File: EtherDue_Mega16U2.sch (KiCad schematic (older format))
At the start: 25 parts, among them IC301 ATMEGA16U2, P301 USB_5PIN_SHELL, X301 TXC 7A 12MHz 18pF

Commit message: Pre-autorouter hand routed traces
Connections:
- net labels added: RD+_CONN, RD-_CONN, USBVCCU2_CONN
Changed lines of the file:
@@
-EESchema Schematic File Version 2  date Thu 06 Jun 2013 17:31:40 EST
+EESchema Schematic File Version 2  date Wed 19 Jun 2013 10:44:48 EST
 LIBS:freetronics_kicad_sch_lib
 LIBS:power
@@
 Sheet 3 6
 Title ""
-Date "6 jun 2013"
+Date "19 jun 2013"
 Rev ""
 Comp ""
@@
 NoConn ~ 8100 2400
 NoConn ~ 8100 2500
+Text Label 2600 4250 2    60   ~ 0
+RD-_CONN
+Text Label 2600 4450 2    60   ~ 0
+RD+_CONN
+Text Label 1450 4150 0    60   ~ 0
+USBVCCU2_CONN
 $EndSCHEMATC

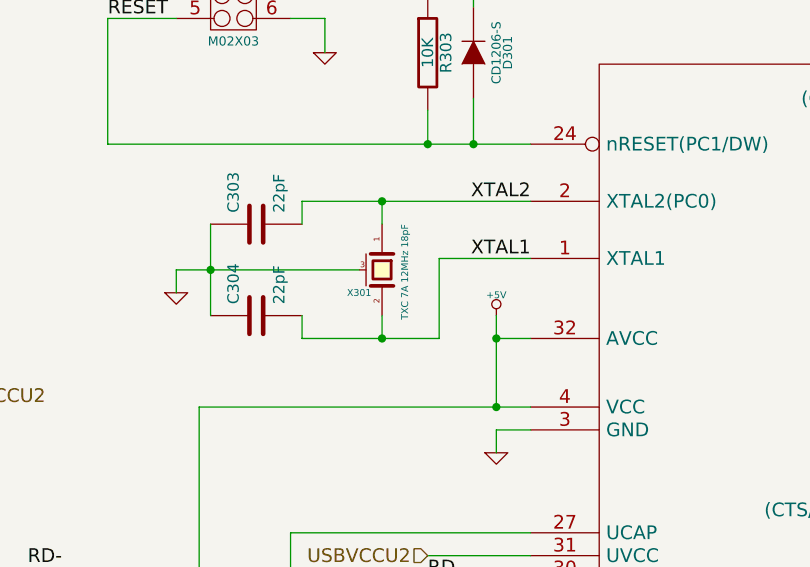
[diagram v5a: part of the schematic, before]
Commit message: Fix ATMega16u2 to run at 16MHz
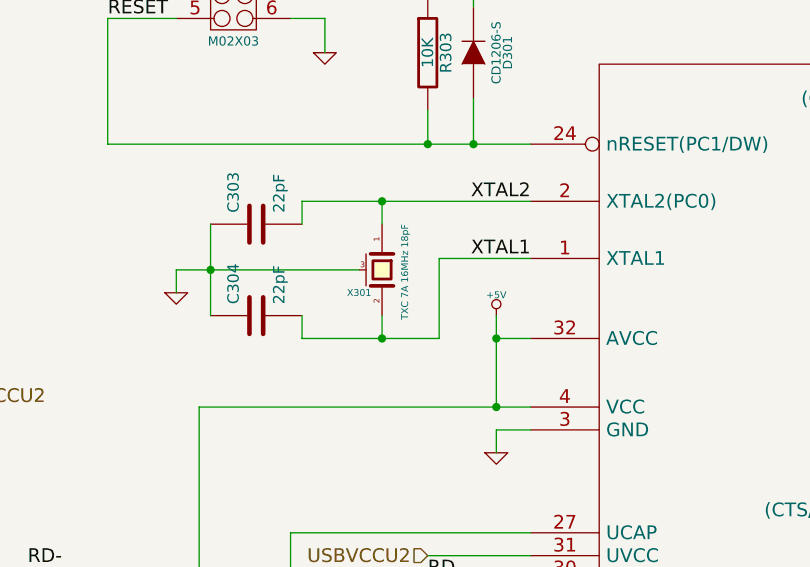
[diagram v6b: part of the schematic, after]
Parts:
- X301: value TXC 7A 12MHz 18pF -> TXC 7A 16MHz 18pF
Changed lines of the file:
@@
 P 4900 2950
 F 0 "X301" V 5000 2850 30  0000 C CNN
-F 1 "TXC 7A 12MHz 18pF" H 4700 3050 30  0000 L CNN
+F 1 "TXC 7A 16MHz 18pF" H 4700 3050 30  0000 L CNN
 F 2 "~" H 4900 2950 60  0000 C CNN
 F 3 "~" H 4900 2950 60  0000 C CNN

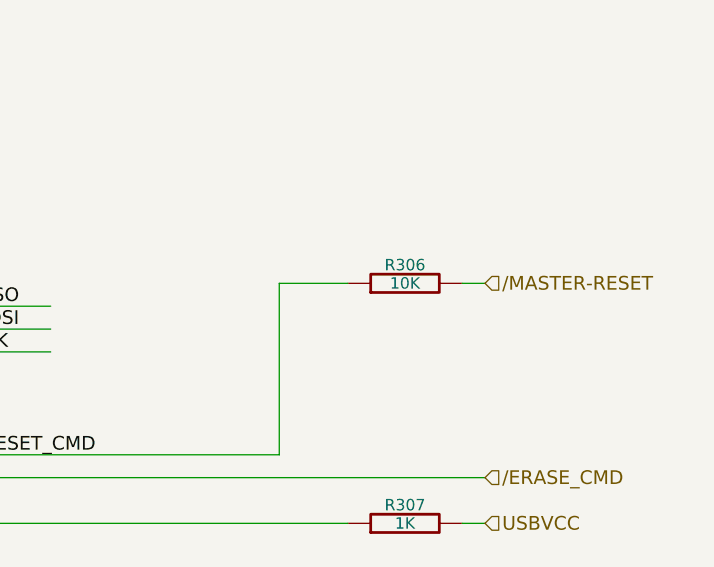
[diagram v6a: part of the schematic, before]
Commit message: Big power fixes: Fix major problem with VDDOUT/1.8V net, rearrange decoupling capacitors
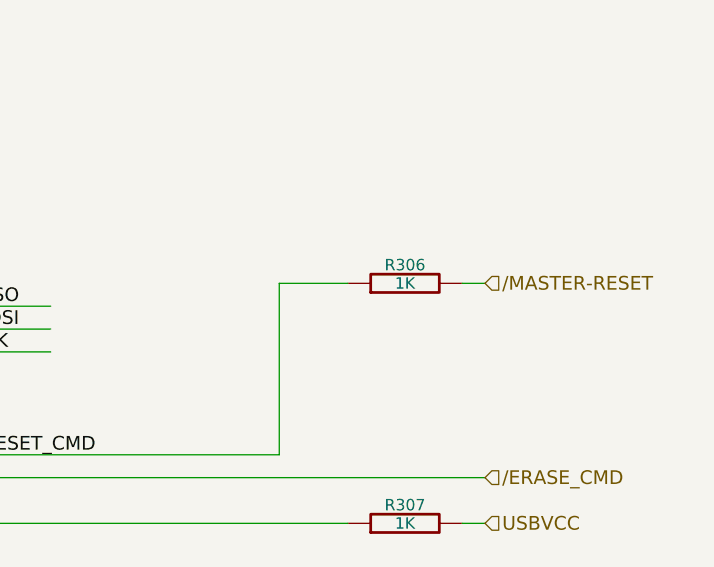
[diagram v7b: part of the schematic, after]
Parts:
- R306: value 10K -> 1K
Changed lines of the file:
@@
 P 10000 2500
 F 0 "R306" V 10080 2500 50  0000 C CNN
-F 1 "10K" V 10000 2500 50  0000 C CNN
+F 1 "1K" V 10000 2500 50  0000 C CNN
 F 2 "" H 10000 2500 60  0001 C CNN
 F 3 "" H 10000 2500 60  0001 C CNN
